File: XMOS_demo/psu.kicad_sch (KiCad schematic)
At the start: 6 parts, among them U3 AP61200Z6

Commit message: sch work
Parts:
- added C26: 33p, Capacitor_SMD:C_0603_1608Metric, symbol Device:C_Small
- added R18: 100k, Resistor_SMD:R_0603_1608Metric, symbol Device:R_Small
- added R19: 200k, Resistor_SMD:R_0603_1608Metric, symbol Device:R_Small
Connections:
- net GND: now also R19.2
- net P0V9: now also C26.1, R18.1
- net P5V0: now also U3.5 (EN)
- net at R15.2, R16.1, U3.1 (FB): now also C26.2, R18.2, R19.1
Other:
- company: (none) -> AGH University
- title: (none) -> USB Sound Card Power Supply
- moved on the sheet: C11, C24, L1, R15, R16, U3

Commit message: Lots of sch work
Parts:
- L1: footprint Inductor_SMD:L_Abracon_ASPI-3012S -> _Inductor_SMD:L_Abracon_ASPI-3012S_3D_Simple
- U3: footprint Package_SO:Diodes_SO-8EP -> Package_TO_SOT_SMD:SOT-563
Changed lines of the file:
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@@
 			)
 		)
-		(property "Footprint" "Inductor_SMD:L_Abracon_ASPI-3012S"
+		(property "Footprint" "_Inductor_SMD:L_Abracon_ASPI-3012S_3D_Simple"
 			(at 115.57 53.34 0)
 			(effects
@@
 			)
 		)
-		(property "Footprint" "Package_SO:Diodes_SO-8EP"
+		(property "Footprint" "Package_TO_SOT_SMD:SOT-563"
 			(at 96.52 44.45 0)
 			(effects

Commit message: sch work, pcb import and initial board outline
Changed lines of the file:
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@@
+	)
+	(junction
+		(at 147.32 50.8)
+		(diameter 0)
+		(color 0 0 0 0)
 	)
 	(junction
@@
 	(wire
 		(pts
+			(xy 147.32 50.8) (xy 157.48 50.8)
+		)
+		(stroke
+			(width 0)
+			(type default)
+		)
+	)
+	(wire
+		(pts
 			(xy 119.38 53.34) (xy 121.92 53.34)
 		)
@@
 	(wire
 		(pts
+			(xy 147.32 48.26) (xy 147.32 50.8)
+		)
+		(stroke
+			(width 0)
+			(type default)
+		)
+	)
+	(wire
+		(pts
 			(xy 132.08 58.42) (xy 132.08 60.96)
 		)
@@
 	(wire
 		(pts
-			(xy 142.24 50.8) (xy 157.48 50.8)
+			(xy 142.24 50.8) (xy 147.32 50.8)
 		)
 		(stroke
@@
 					(unit 1)
 				)
+			)
+		)
+	)
+	(symbol
+		(lib_id "power:PWR_FLAG")
+		(at 147.32 48.26 0)
+		(unit 1)
+		(exclude_from_sim no)
+		(in_bom yes)
+		(on_board yes)
+		(dnp no)
+		(property "Reference" "#FLG03"
+			(at 147.32 46.355 0)
+			(effects
+				(font
+					(size 1.27 1.27)
+				)
+				(hide yes)
+			)
+		)
+		(property "Value" "PWR_FLAG"
+			(at 147.32 44.704 0)
+			(effects
+				(font
+					(size 1.016 1.016)
+				)
+			)
+		)
+		(property "Footprint" ""
+			(at 147.32 48.26 0)
+			(effects
+				(font
+					(size 1.27 1.27)
+				)
+				(hide yes)
+			)
+		)
+		(property "Datasheet" "~"
+			(at 147.32 48.26 0)
+			(effects
+				(font
+					(size 1.27 1.27)
+				)
+				(hide yes)
+			)
+		)
+		(property "Description" "Special symbol for telling ERC where power comes from"
+			(at 147.32 48.26 0)
+			(effects
+				(font
+					(size 1.27 1.27)
+				)
+				(hide yes)
+			)
+		)
+		(pin "1"
+		)
+		(instances
+			(project "XMOS_demo"
+				(path "/0a855fb0-ca19-4770-811e-70d8770d7fdd/13d4ac51-413b-4f8b-9448-517b4883a5ce"
+					(reference "#FLG03")
+					(unit 1)
+				)

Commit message: sch mostly finished, needs tp, pcb component layout started
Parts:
- added C24, C25, C26, C27: 22u, Capacitor_SMD:C_1206_3216Metric, symbol Device:C_Small
- added J9: Conn_01x05, Connector_PinHeader_2.54mm:PinHeader_1x05_P2.54mm_Vertical, symbol Connector_Generic:Conn_01x05
- added R22, R23, R24: 0R, Resistor_SMD:R_0603_1608Metric, symbol Device:R_Small
- added U4: TLV75733PDBV, Package_TO_SOT_SMD:SOT-23-5, symbol Regulator_Linear:TLV75733PDBV
- added U5: TLV75718PDBV, Package_TO_SOT_SMD:SOT-23-5, symbol Regulator_Linear:TLV75718PDBV
- renumbered C26 to C28, C11 to C29, C24 to C30, R15 to R25, R18 to R26, R16 to R27, R19 to R28, U3 to U6
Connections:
- net GND: now also C24.2, C25.2, C26.2, C27.2, J9.5 (Pin_5), U4.2 (GND), U5.2 (GND)
- net P0V9: now also J9.4 (Pin_4)
- net P5V0: now also C24.1, C26.1, J9.1 (Pin_1), R22.1, R23.1, R24.1, U4.1 (IN), U5.1 (IN); no longer U6.5 (EN)
- new net: R24.2, U6.5 (EN)
- new net: R22.2, U4.3 (EN)
- new net: R23.2, U5.3 (EN)
- new net P1V8: C27.1, J9.3 (Pin_3), U5.5 (OUT)
- new net P3V3: C25.1, J9.2 (Pin_2), U4.5 (OUT)
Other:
- moved on the sheet: C28, C29, C30, L1, R25, R26, R27, R28, U6

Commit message: finished sch, pcb work
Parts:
- removed J9: Conn_01x05, Connector_PinHeader_2.54mm:PinHeader_1x05_P2.54mm_Vertical, symbol Connector_Generic:Conn_01x05
- added TP5, TP6, TP7, TP8: TestPoint, TestPoint:TestPoint_Keystone_5005-5009_Compact, symbol Connector:TestPoint
- C29: footprint Capacitor_SMD:C_1206_3216Metric -> Capacitor_SMD:C_0805_2012Metric; Max Voltage 16V -> 10V
- renumbered R22 to R20, R23 to R21, R24 to R22, R25 to R23, R26 to R24, R27 to R25, R28 to R26
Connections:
- net P0V9: now also TP8.1
- net P1V8: now also TP7.1
- net P3V3: now also TP6.1
- net P5V0: now also TP5.1

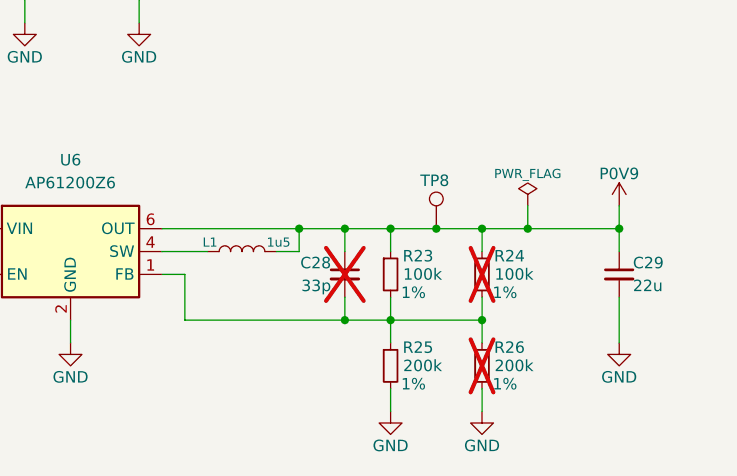
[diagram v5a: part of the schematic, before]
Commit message: PCB work, changes for better routing
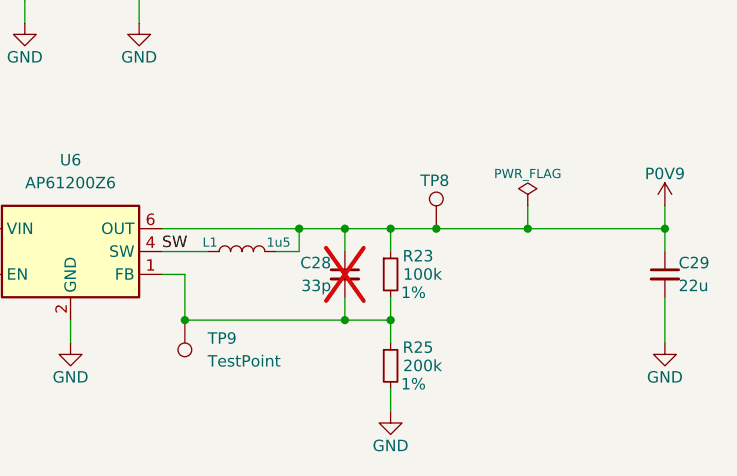
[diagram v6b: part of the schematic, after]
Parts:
- removed R24: 100k, Resistor_SMD:R_0603_1608Metric, symbol Device:R_Small
- removed R26: 200k, Resistor_SMD:R_0603_1608Metric, symbol Device:R_Small
- added TP9: TestPoint, TestPoint:TestPoint_Pad_D2.0mm, symbol Connector:TestPoint
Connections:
- net at C28.2, R23.2, R25.1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: now also TP9.1
- net SW: now reaches L1.1, U6.4 (SW)
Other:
- moved on the sheet: C29

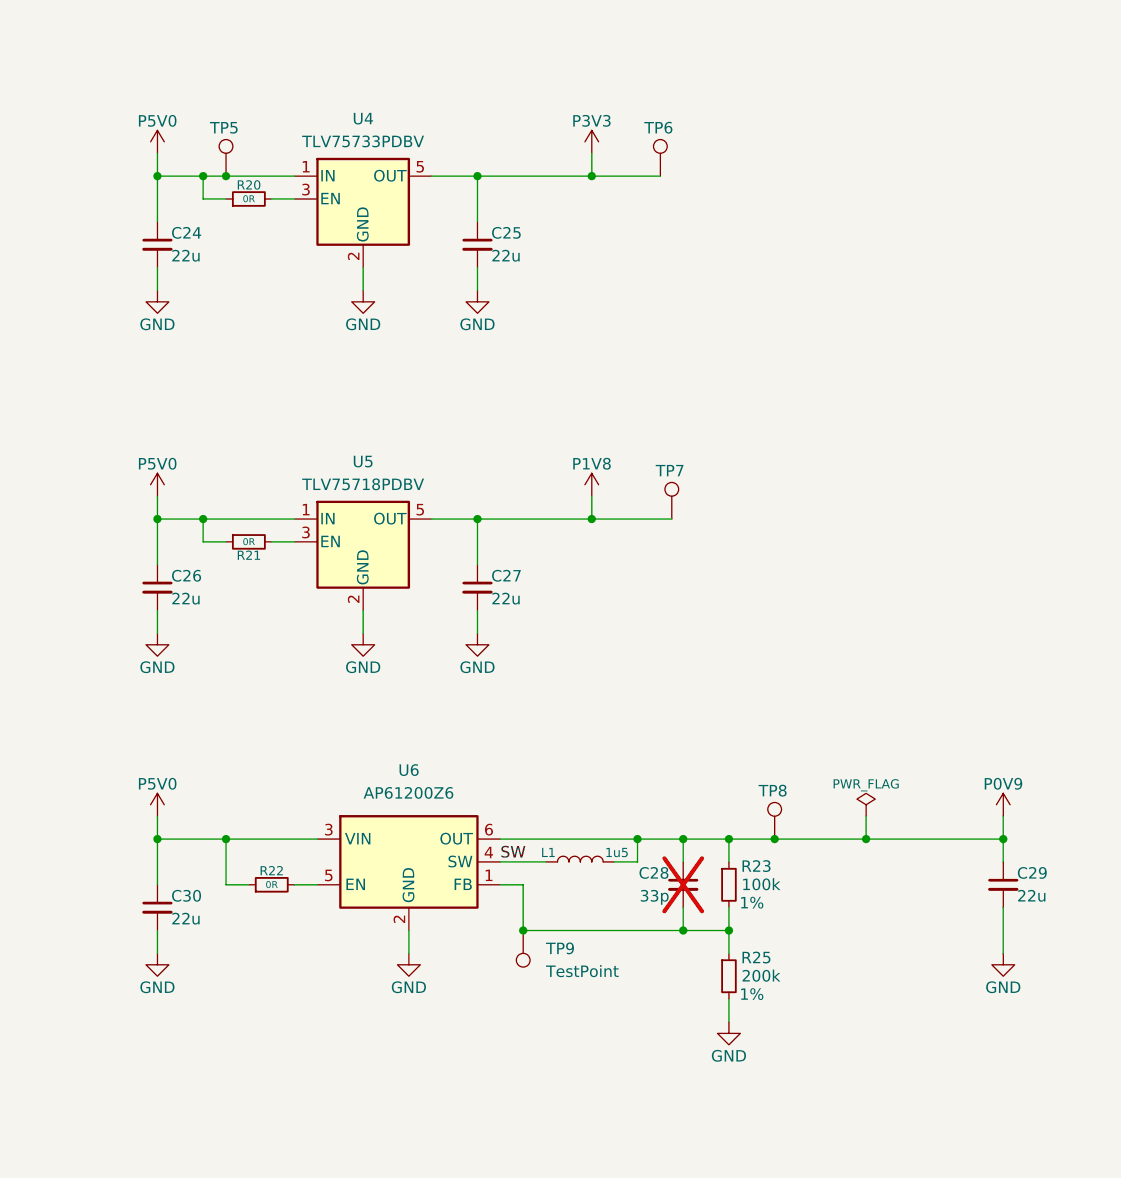
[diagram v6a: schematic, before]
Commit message: sch work changes (jumpers, connectors, tp)
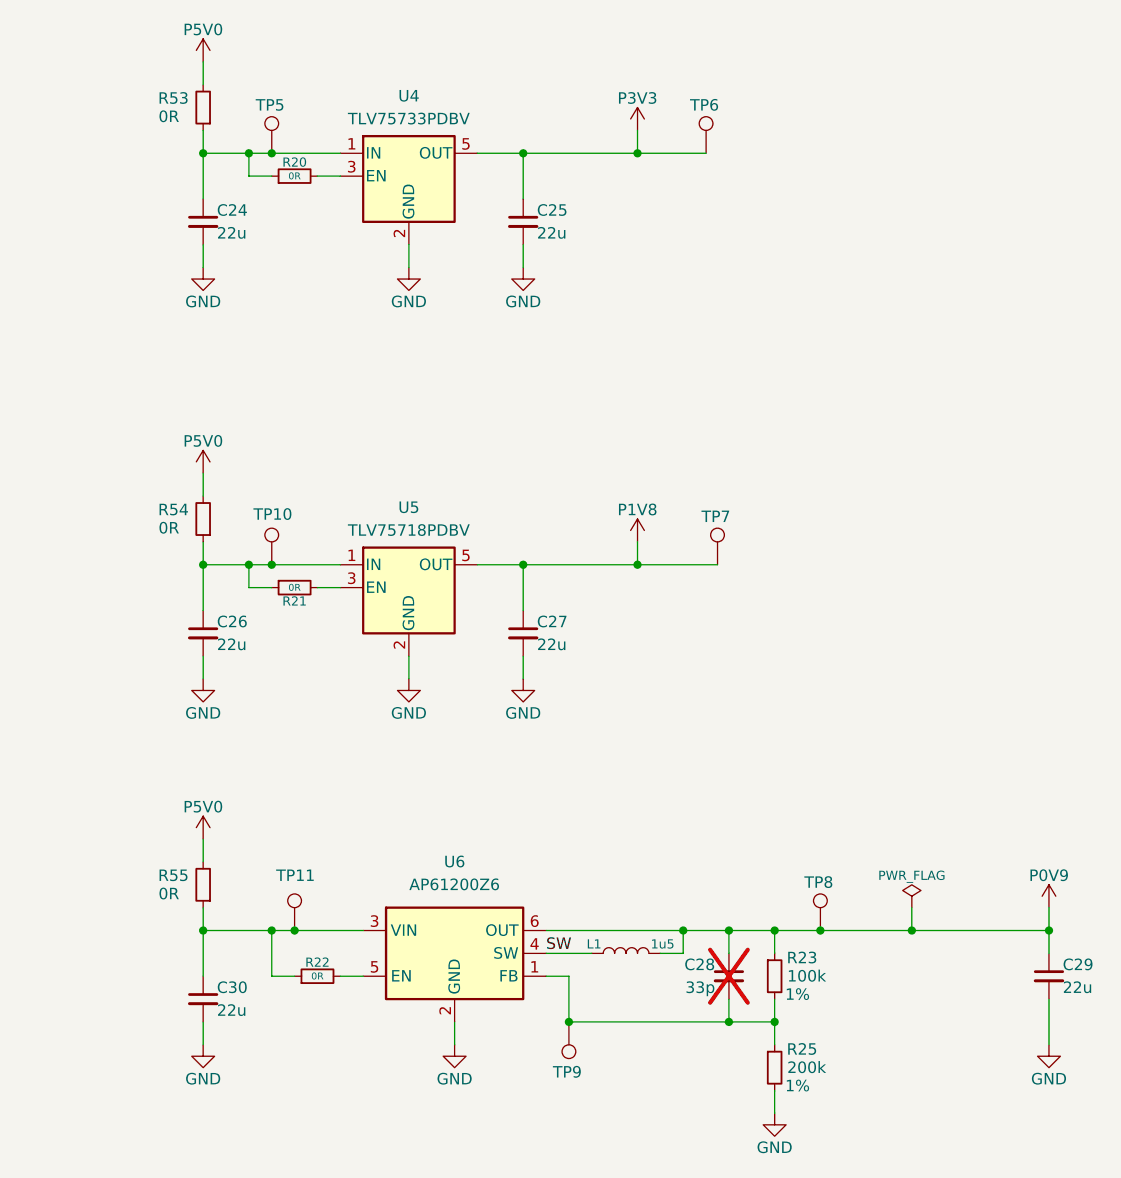
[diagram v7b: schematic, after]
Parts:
- added R53, R54, R55: 0R, Resistor_SMD:R_0603_1608Metric, symbol Device:R_Small
- added TP10, TP11: TestPoint, TestPoint:TestPoint_Pad_D2.0mm, symbol Connector:TestPoint
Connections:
- net P5V0: now also R53.2, R54.2, R55.2; no longer C24.1, C26.1, C30.1, R20.1, R21.1, R22.1, TP5.1, U4.1 (IN), U5.1 (IN), U6.3 (VIN)
- new net: C24.1, R20.1, R53.1, TP5.1, U4.1 (IN)
- new net: C30.1, R22.1, R55.1, TP11.1, U6.3 (VIN)
- new net: C26.1, R21.1, R54.1, TP10.1, U5.1 (IN)
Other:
- moved on the sheet: C24, C25, C26, C27, C28, C29, C30, L1, R20, R21, R22, R23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

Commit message: pcb routing
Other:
- moved on the sheet: C24, C26, C30, R53, R54, R55, TP10, TP11, TP5
